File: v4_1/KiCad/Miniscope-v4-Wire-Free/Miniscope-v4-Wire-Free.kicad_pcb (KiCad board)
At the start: 6 copper layers, 25 x 13 mm, 91 parts, among them J1 0475710001, J10 Conn_01x01, J2 Conn_01x04, J3 Conn_01x04, J4 Conn_01x01, J5 Conn_01x01, J6 Conn_01x01, J7 Conn_01x01, J8 Conn_01x01, J9 Conn_01x01, Q1 NTK3134NT1G, U1 LTC3554, U2 HV892, U3 LTC3218, U4 MAX13030EETE+BGA, U5 TSOP57438TT1, U6 ATSAMD51J20A-UUT-EFP, U7 NCP163AMX330TBG, U8 NOIP1SN0480A, U9 LMV321IDCKR, Y1 Crystal_GND24, Y2 Crystal_GND24

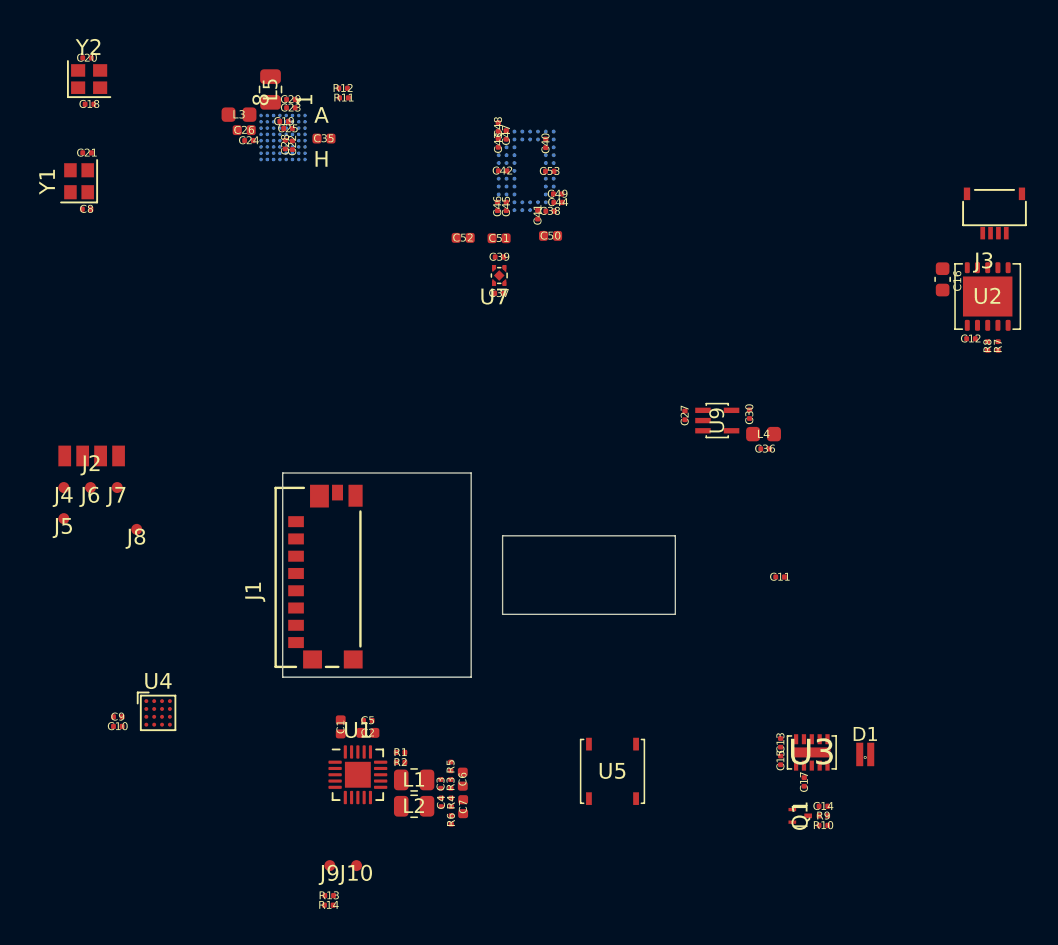
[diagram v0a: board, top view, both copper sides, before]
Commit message: Start routing PCB v4 wire-free
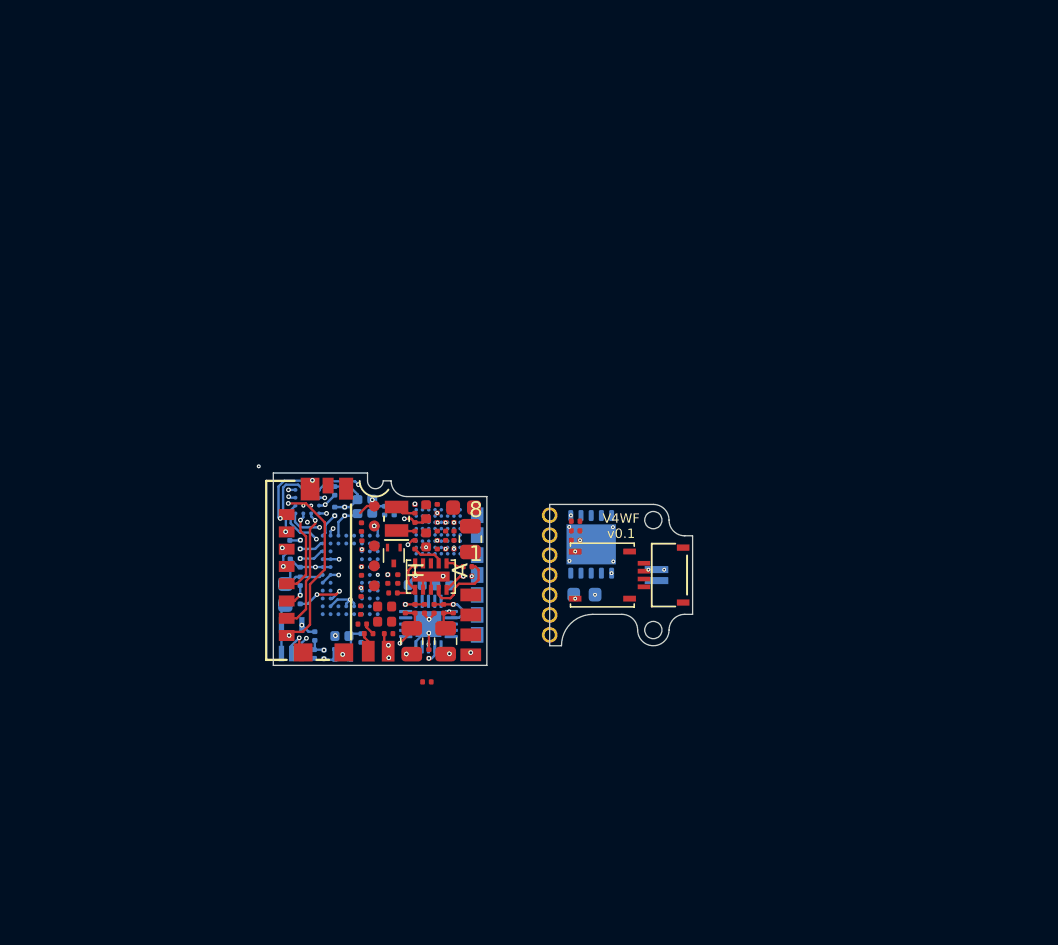
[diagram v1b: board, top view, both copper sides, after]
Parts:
- removed C21, C8: 26pF, .Capacitor:C_0201_0603Metric_L
- removed C39: 1uF, .Capacitor:C_0201_0603Metric_L
- removed Y1: Crystal_GND24, Crystal:Crystal_SMD_2016-4Pin_2.0x1.6mm
- added J14: Conn_01x01, .Connector:Conn_1x1_700_Circular_Pad, B.Cu at (92.4, 60.7)
- added J15: Conn_01x01, .Connector:Conn_1x1_700_Circular_Pad, B.Cu at (92.4, 62.0)
- added J16: Conn_01x01, .Connector:Conn_1x1_700_Circular_Pad, B.Cu at (92.4, 63.2)
- added J17: Conn_01x01, .Connector:Conn_1x1_700_Circular_Pad, B.Cu at (92.4, 64.5)
- added J18: Conn_01x01, .Connector:Conn_1x1_700_Circular_Pad, B.Cu at (92.4, 65.8)
- added J19: Conn_01x01, .Connector:Conn_1x1_700_Circular_Pad, B.Cu at (92.4, 67.0)
- added J20: Conn_01x01, .Connector:Conn_1x1_700_Circular_Pad, B.Cu at (92.4, 68.3)
- added J21: Conn_01x01, .Connector:Conn_1x1_700_Circular_Pad, F.Cu at (97.0, 60.7)
- added J22: Conn_01x01, .Connector:Conn_1x1_700_Circular_Pad, F.Cu at (97.0, 62.0)
- added J23: Conn_01x01, .Connector:Conn_1x1_700_Circular_Pad, F.Cu at (97.0, 63.2)
- added J24: Conn_01x01, .Connector:Conn_1x1_700_Circular_Pad, F.Cu at (97.0, 64.5)
- added J25: Conn_01x01, .Connector:Conn_1x1_700_Circular_Pad, F.Cu at (97.0, 65.8)
- added J26: Conn_01x01, .Connector:Conn_1x1_700_Circular_Pad, F.Cu at (97.0, 67.0)
- added J27: Conn_01x01, .Connector:Conn_1x1_700_Circular_Pad, F.Cu at (97.0, 68.3)
- added Mount: Conn_1x1_700_Circular_Pad, .Connector:Conn_1x1_700_Circular_Pad, F.Cu at (103.6, 61.0)
- added Mount: Conn_1x1_700_Circular_Pad, .Connector:Conn_1x1_700_Circular_Pad, F.Cu at (103.6, 68.0)
- C10, C11, C16, C27, C30, C36, C37, C38, C40, C41, C44, C48, C49, C50, C51, C52, C53, C6, C7, C9, D1, L4, R11, R12, U1, U2, U4, U7, U9: moved to B.Cu
- R13: value 200K -> 400K
- Y2: value Crystal_GND24 -> Crystal; footprint Crystal:Crystal_SMD_2016-4Pin_2.0x1.6mm -> Crystal:Crystal_SMD_MicroCrystal_CC8V-T1A-2Pin_2.0x1.2mm
- moved C20 35.5 mm to (88.4, 60.3), turned to 90 degrees
- moved Y2 34.2 mm to (87.3, 60.9), turned to 90 degrees
- moved C18 34.0 mm to (88.4, 61.4), turned to 90 degrees
- moved C48 33.7 mm to (85.0, 68.5), turned to 270 degrees
- moved C40 33.0 mm to (81.1, 66.1)
- moved L4 32.1 mm to (80.2, 65.7), turned to 90 degrees
- moved C47 31.6 mm to (85.0, 66.7), turned to 90 degrees
- moved L5 31.3 mm to (91.9, 62.2), turned to 90 degrees
- moved C14 31.3 mm to (86.7, 64.8), turned to 90 degrees
- moved C11 31.3 mm to (80.5, 62.6), turned to 90 degrees
- moved J3 31.2 mm to (103.0, 64.5), turned to 90 degrees
- moved R10 31.1 mm to (87.0, 65.6), turned to 180 degrees
- moved C36 31.1 mm to (80.5, 63.7), turned to 90 degrees
- moved C30 31.1 mm to (82.0, 68.4)
- moved R9 31.0 mm to (87.3, 64.8), turned to 90 degrees
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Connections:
- net Net-(D1-PadA) renamed /I_LED
- C12 pad 1: VDC -> +3V3
- J1 pad P6: Net-(J1-PadP6) -> GND
- J2 pad 2: /USB_DP -> /UART_TX
- J2 pad 3: /USB_DM -> /UART_RX
- U2 pad 2: VDC -> +3V3
- U4 pad C4: /SD_EN -> +1V8
- U6 pad D1: Net-(U6-PadD1) -> /UART_RX
- U6 pad D4: Net-(U6-PadD4) -> /UART_TX
- Y2 pad 2: GND -> /XOUT32
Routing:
- net GND: track 0.00 -> 30.8 mm, vias 0 -> 44
- net +3V3: track 0.00 -> 14.2 mm, vias 0 -> 10
- net +1V8: track 0.00 -> 13.8 mm, vias 0 -> 5
- net /SD_DAT1: track 0.00 -> 13.2 mm, vias 0 -> 3
- net /SD_DAT0: track 0.00 -> 7.92 mm, vias 0 -> 1
- net /SD_CLK: track 0.00 -> 5.59 mm, vias 0 -> 1
- net Net-(C15-Pad2): track 0.00 -> 4.80 mm
- net /SD_DAT2: track 0.00 -> 4.59 mm, vias 0 -> 1
- net /SD_DAT3: track 0.00 -> 4.39 mm, vias 0 -> 2
- net Net-(C3-Pad2): track 0.00 -> 4.21 mm, vias 0 -> 2
- net /SD_CMD: track 0.00 -> 3.75 mm, vias 0 -> 2
- net /VREF_BOTPLATE: track 0.00 -> 3.35 mm
- net /I_SET: track 0.00 -> 3.26 mm
- net Net-(L4-Pad1): track 0.00 -> 3.20 mm
- net Net-(C4-Pad2): track 0.00 -> 3.04 mm, vias 0 -> 1
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- added copper zone on In1.Cu, net GND
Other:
- board size 25 x 13 mm -> 26.7 x 12.2 mm
- net class Default: clearance 0.0762 -> 0.1016
- rule trace_clearance: 0.0762 -> 0.1016
- board text added: "V4WF v0.1"

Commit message: Do more routing
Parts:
- added D2: LED_Small_ALT, .LED:LED_SC80X160X65L40L, F.Cu at (86.0, 69.6)
- added D3: LED_Small_ALT, .LED:LED_SC80X160X65L40L, F.Cu at (99.5, 63.6)
- added J11: Conn_01x01, .Connector:Conn_1x1_700_Circular_Pad, B.Cu at (92.4, 68.9)
- added J12: Conn_01x01, .Connector:Conn_1x1_700_Circular_Pad, F.Cu at (97.0, 68.9)
- added R15: 37K, .Resistor:R_0201_0603Metric_ERJ_L, F.Cu at (101.4, 63.9)
- added R16: 100K, .Resistor:R_0201_0603Metric_ERJ_L, F.Cu at (87.4, 71.2)
- added R17: 25K, .Resistor:R_0201_0603Metric_ERJ_L, F.Cu at (91.9, 71.8)
- added R18: R_Small_US, .Resistor:R_0201_0603Metric_ERJ_L, F.Cu at (101.4, 63.3)
- added SW1: TL3780AF330QG, .Switch:SMD-Switch-3mmx2mm, F.Cu at (99.9, 61.1)
- J10, J9: moved to B.Cu
- R11, R12: moved to F.Cu
- moved R2 3.58 mm to (86.6, 68.8), turned to 0 degrees
- moved R7 3.20 mm to (101.4, 62.7)
- moved R11 2.41 mm to (85.0, 59.2), turned to 90 degrees
- moved U5 2.05 mm to (100.0, 66.5), turned to 180 degrees
- moved R8 1.86 mm to (100.2, 62.7)
- moved R12 1.48 mm to (85.0, 60.3)
- moved U6 0.69 mm to (89.4, 62.2)
- moved J26 0.64 mm to (97.0, 66.4)
- moved J27 0.64 mm to (97.0, 67.7)
- moved J21 0.63 mm to (97.0, 60.1)
- moved J22 0.63 mm to (97.0, 61.3)
- moved J23 0.63 mm to (97.0, 62.6)
- moved J24 0.63 mm to (97.0, 63.9)
- moved J25 0.63 mm to (97.0, 65.1)
- moved J20 0.63 mm to (92.4, 67.7)
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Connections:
- net /XOUT renamed Net-(U6-PadA3)
- net Net-(U6-PadD8) renamed /LED_STATUS
- J1 pad G4: Net-(J1-PadG4) -> GND
- J1 pad G5: Net-(J1-PadG5) -> /SD_DET
- J10 pad 1: GND -> /BAT+
- J20 pad 1: GND -> /nON
- J27 pad 1: GND -> /nON
- J4 pad 1: GND -> /SWDIO
- J5 pad 1: /SWCLK -> GND
- J6 pad 1: /SWDIO -> +1V8
- J7 pad 1: +1V8 -> /SWCLK
- J9 pad 1: /BAT+ -> GND
- U1 pad 10: Net-(U1-Pad10) -> /STBY_POWER
- U1 pad 2: Net-(U1-Pad2) -> GND
- U1 pad 3: Net-(U1-Pad3) -> /PUSH_BUT_MCU
- U1 pad 5: Net-(U1-Pad5) -> /nON
- U1 pad 8: Net-(U1-Pad8) -> +3V3
- U1 pad 9: Net-(U1-Pad9) -> +1V8
- U6 pad A1: /USB_D+ -> /PUSH_BUT_MCU
- U6 pad A2: /XIN -> /IR_REC
- U6 pad B1: /USB_D- -> /STBY_POWER
- U6 pad F8: Net-(U6-PadF8) -> /SD_DET
- U6 pad G8: Net-(U6-PadG8) -> /MONITOR0
- U6 pad H2: Net-(U6-PadH2) -> /TRIGGER0
- U6 pad H4: Net-(U6-PadH4) -> /RESET_N
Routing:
- net /MONITOR0: track 0.00 -> 13.1 mm, vias 0 -> 2
- net GND: track 30.8 -> 41.2 mm, vias 44 -> 37
- net /SDMMC1_CMD: track 0.46 -> 10.4 mm, vias 1 -> 2
- net /SDMMC1_D3: track 0.44 -> 9.64 mm, vias 1 -> 2
- net /SPI1_MOSI: track 0.00 -> 8.84 mm, vias 0 -> 3
- net /PCC_DEN1: track 0.00 -> 8.24 mm, vias 0 -> 2
- net /PCC_DATA7: track 0.00 -> 8.19 mm, vias 0 -> 3
- net /SPI1_MISO: track 0.00 -> 7.39 mm, vias 0 -> 3
- net /SWDIO: track 0.00 -> 7.24 mm, vias 0 -> 2
- net /SWCLK: track 0.00 -> 7.12 mm, vias 0 -> 2
- net +3V3: track 14.2 -> 21.0 mm, vias 10 -> 13
- net /SDMMC1_D1: track 0.37 -> 7.02 mm, vias 1 -> 2
- net /SDMMC1_D0: track 0.48 -> 7.01 mm, vias 1 -> 2
- net /SDMMC1_CK: track 2.26 -> 8.69 mm, vias 1 -> 2
- net /SPI1_SCK: track 0.00 -> 6.40 mm, vias 0 -> 4
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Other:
- outline, holes or cut-outs redrawn
- rule pad_to_mask_clearance: 0.05 -> 0.0254

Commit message: Finish most of the routing.
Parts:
- added Q2: MMBT3904LP-7B, .Transistor:TRXDFN3_101X61X53L25X15N, B.Cu at (85.3, 58.7)
- added R19: 1K, .Resistor:R_0201_0603Metric_ERJ_L, B.Cu at (86.6, 60.4)
- added R20: 100K, .Resistor:R_0201_0603Metric_ERJ_L, F.Cu at (89.3, 68.1)
- R16, R17: moved to B.Cu
- moved R16 7.13 mm to (91.4, 65.4), turned to 90 degrees
- moved R17 6.48 mm to (86.5, 68.2), turned to 180 degrees
- moved C15 0.47 mm to (92.0, 64.3), turned to 270 degrees
- moved C13 0.42 mm to (91.4, 64.3), turned to 90 degrees
- moved R10 0.13 mm to (87.0, 65.6)
- moved D2 0.11 mm to (86.1, 69.6), turned to 180 degrees
- moved C14 0.09 mm to (87.0, 65.0)
- moved R9 0.06 mm to (87.0, 64.4)
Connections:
- D2 pad 2: VDC -> Net-(D2-Pad2)
- J15 pad 1: +1V8 -> /I2C_BB_SCL
- J16 pad 1: /I_LED -> /I2C_BB_SDA
- J17 pad 1: /I2C_BB_SCL -> /IR_REC
- J18 pad 1: /I2C_BB_SDA -> /I_LED
- J19 pad 1: /IR_REC -> +1V8
- J2 pad 2: /UART_TX -> /UART_RX
- J2 pad 3: /UART_RX -> /UART_TX
- J22 pad 1: +1V8 -> /I2C_BB_SCL
- J23 pad 1: /I_LED -> /I2C_BB_SDA
- J24 pad 1: /I2C_BB_SCL -> /IR_REC
- J25 pad 1: /I2C_BB_SDA -> /I_LED
- J26 pad 1: /IR_REC -> +1V8
- R2 pad 1: Net-(D2-Pad1) -> Net-(D2-Pad2)
- R2 pad 2: Net-(R2-Pad2) -> VDC
- U1 pad 10: /STBY_POWER -> GND
- U1 pad 14: Net-(R2-Pad2) -> /nCHRG
- U1 pad 8: +3V3 -> /3V3_EN
- U6 pad A3: Net-(U6-PadA3) -> /nCHRG
- U6 pad B1: /STBY_POWER -> /3V3_EN
- U6 pad D8: /LED_STATUS -> /SD_DET
- U6 pad F8: /SD_DET -> /LED_STATUS
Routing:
- net /ADC0: track 0.84 -> 19.9 mm, vias 1 -> 3
- net +1V8: track 16.6 -> 34.5 mm
- net Net-(D2-Pad1): track 0.95 -> 15.0 mm, vias 0 -> 3
- net VDC: track 2.49 -> 16.1 mm, vias 2 -> 4
- net /nCHRG: track 0.00 -> 12.7 mm, vias 0 -> 3
- net /I_LED: track 0.00 -> 12.3 mm, vias 0 -> 3
- net /nON: track 0.00 -> 11.0 mm, vias 0 -> 1
- net /USB_VBUS: track 0.00 -> 8.57 mm, vias 0 -> 2
- net /nRESET: track 0.00 -> 7.91 mm, vias 1 -> 2
- net /UART_TX: track 0.00 -> 7.79 mm, vias 2 -> 3
- net GND: track 41.2 -> 48.9 mm, vias 37 -> 38
- net /IR_REC: track 1.05 -> 7.70 mm, vias 0 -> 1
- net /UART_RX: track 0.00 -> 6.34 mm, vias 0 -> 4
- net /I2C_BB_SDA: track 2.19 -> 8.34 mm, vias 1 -> 3
- net /LED_PWM: track 0.00 -> 5.61 mm, vias 0 -> 2
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- added copper zone on In4.Cu, net +3V3
- added copper zone on B.Cu, net GND
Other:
- outline, holes or cut-outs redrawn

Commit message: routing almost done.
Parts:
- moved J11 0.05 mm to (92.3, 68.9)
- moved J14 0.05 mm to (92.3, 60.1)
- moved J15 0.05 mm to (92.3, 61.3)
- moved J16 0.05 mm to (92.3, 62.6)
- moved J17 0.05 mm to (92.3, 63.9)
- moved J18 0.05 mm to (92.3, 65.1)
- moved J19 0.05 mm to (92.3, 66.4)
- moved J20 0.05 mm to (92.3, 67.7)
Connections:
- J3 pad 1: Net-(J3-Pad1) -> /EWL_2
- J3 pad 4: Net-(J3-Pad4) -> /EWL_1
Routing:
- net +1V8: track 34.5 -> 55.0 mm, vias 13 -> 22
- net GND: track 48.9 -> 62.8 mm, vias 38 -> 44
- net /VDD_PIX: track 3.95 -> 16.9 mm, vias 2 -> 4
- net +3V3: track 20.9 -> 29.7 mm, vias 12 -> 22
- net /VDDCORE: track 1.05 -> 3.03 mm
- net /ADC0: track 19.9 -> 18.1 mm
- net /VDDA: track 0.79 -> 2.55 mm
- net /SDMMC1_D2: track 8.56 -> 9.32 mm
- net /SDMMC1_CK: track 8.69 -> 9.42 mm
- net /EWL_2: track 3.41 -> 3.91 mm
- net /EWL_1: track 5.00 -> 5.50 mm
- added copper zone on In2.Cu, net +1V8
- added copper zone on In3.Cu, net +3V3

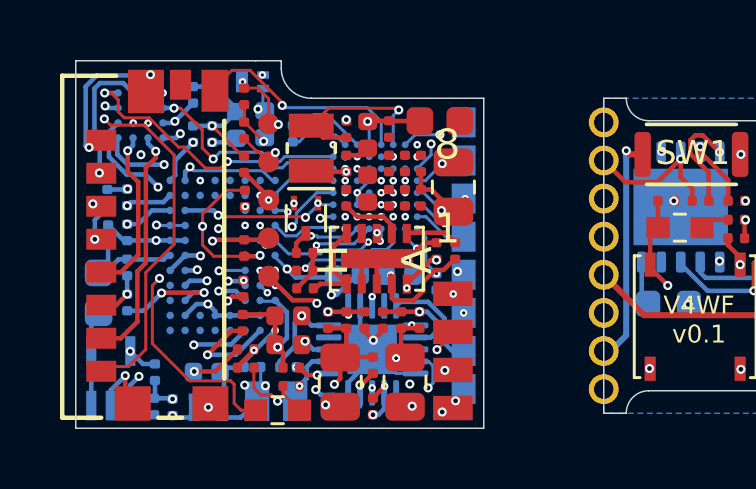
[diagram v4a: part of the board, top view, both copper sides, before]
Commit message: First routing pass finished. Need to check everything.
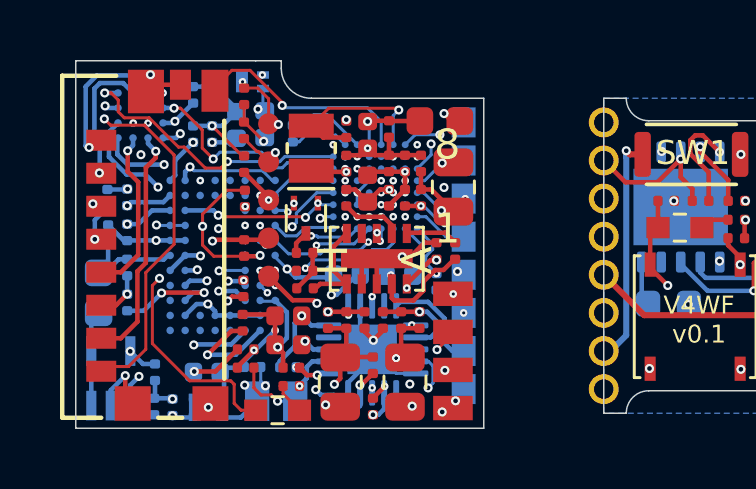
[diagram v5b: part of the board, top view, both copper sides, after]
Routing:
- net +1V8: track 55.0 -> 65.7 mm, vias 22 -> 27
- net GND: track 62.8 -> 72.6 mm, vias 44 -> 47
- net +3V3: track 29.7 -> 34.8 mm, vias 22 -> 24
- net /UART_TX: track 7.52 -> 9.68 mm
- net /ADC0: track 18.1 -> 18.7 mm

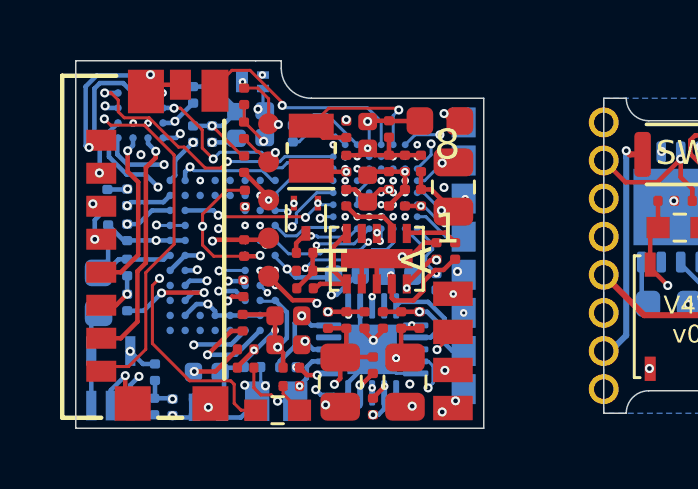
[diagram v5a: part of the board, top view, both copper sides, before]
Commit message: Pass initial DRC
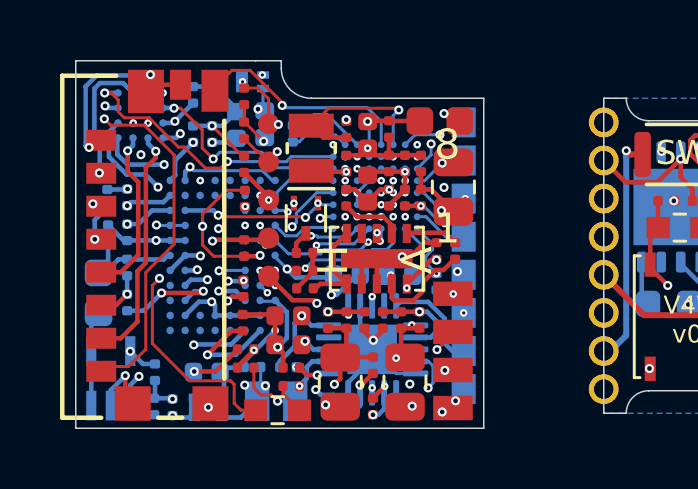
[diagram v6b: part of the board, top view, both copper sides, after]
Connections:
- U2 pad 11: (no net) -> GND
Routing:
- net +3V3: track 34.8 -> 37.0 mm
- net /VREF_BOTPLATE: track 3.35 -> 3.97 mm

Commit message: Minor corrections
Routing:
- net /nCHRG: track 12.7 -> 13.3 mm
- net /EWL_1: vias 2 -> 1

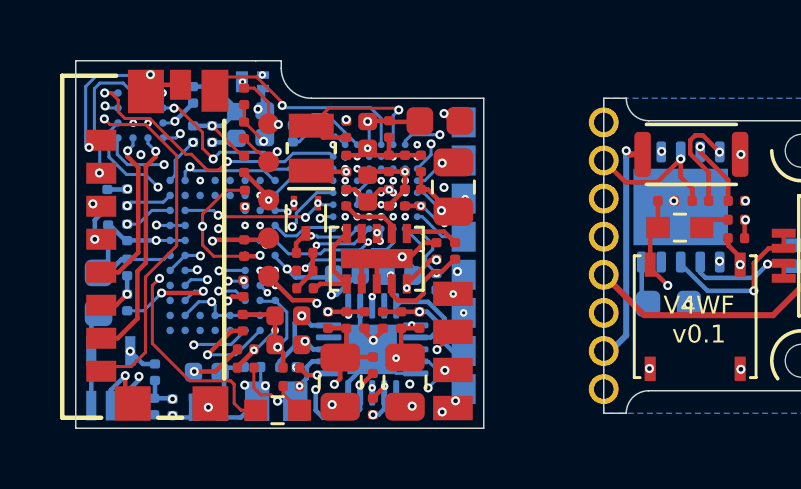
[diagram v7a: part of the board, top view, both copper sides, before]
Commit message: Add frame valid additional pin and external int to MCU.
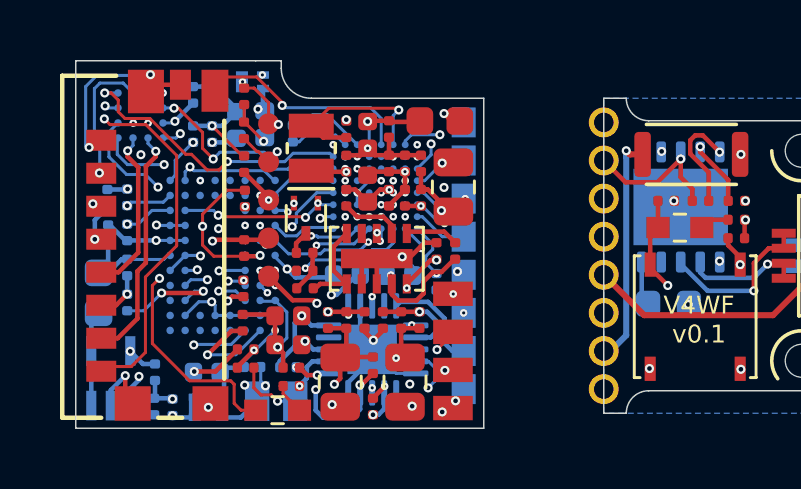
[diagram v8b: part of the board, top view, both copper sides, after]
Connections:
- U2 pad 11: GND -> (no net)
- U6 pad G3: Net-(U6-PadG3) -> /PCC_DEN1
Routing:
- net /PCC_DEN1: track 8.30 -> 8.86 mm
